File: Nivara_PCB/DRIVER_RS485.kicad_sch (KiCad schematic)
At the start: 0 parts

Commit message: Cambios en el RS485
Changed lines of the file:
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@@
 	(generator_version "9.0")
 	(paper "A4")
+	(hierarchical_label "+3.3V"
+		(shape output)
+		(at 86.36 50.8 0)
+		(effects
+			(font
+				(size 1.27 1.27)
+			)
+			(justify left)
+		)
+	)
 	(hierarchical_label "UART_IN"
 		(shape input)
@@
 		)
 	)
+	(hierarchical_label "+5V"
+		(shape output)
+		(at 73.66 50.8 0)
+		(effects
+			(font
+				(size 1.27 1.27)
+			)
+			(justify left)
+		)
+	)
 	(hierarchical_label "RS485_A"
 		(shape bidirectional)
-		(at 49.53 68.58 0)
+		(at 99.06 60.96 0)
 		(effects
 			(font
@@
 	(hierarchical_label "RS485_B"
 		(shape bidirectional)
-		(at 49.53 71.12 0)
+		(at 99.06 63.5 0)
 		(effects
 			(font

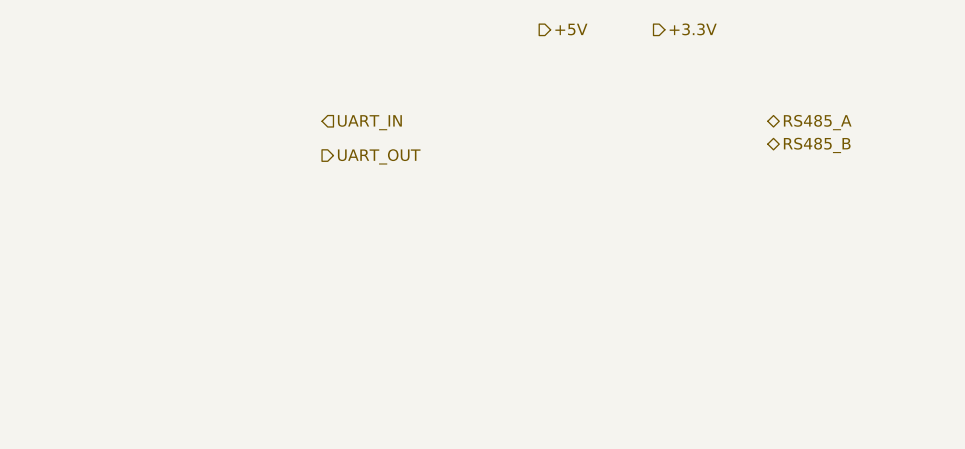
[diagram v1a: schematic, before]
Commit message: Ajuste de RS-485 y protección de alimentación contra cortocircuito y sobre voltaje.
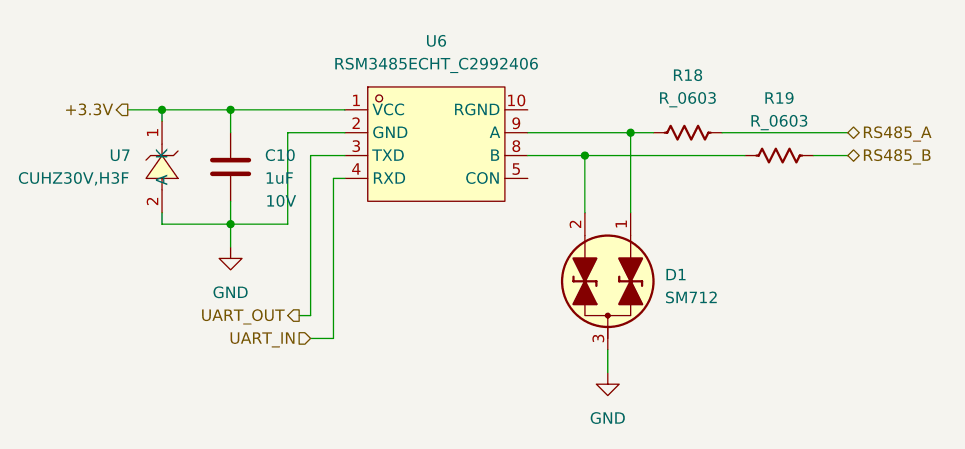
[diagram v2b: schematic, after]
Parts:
- added C10: 1uF, PCM_Capacitor_SMD_AKL:C_0603_1608Metric, symbol PCM_Capacitor_US_AKL:C_0603
- added D1: SM712, PCM_Package_TO_SOT_SMD_AKL:SOT-23, symbol PCM_Diode_TVS_AKL:SM712
- added R18, R19: R_0603, PCM_Resistor_SMD_AKL:R_0603_1608Metric, symbol PCM_Resistor_US_AKL:R_0603
- added U6: RSM3485ECHT_C2992406, EasyEDA:COMM-TH_8P-L19.5-W16.5-P2.54-BL, symbol Fuse_Holder:RSM3485ECHT_C2992406
- added U7: CUHZ30V,H3F, Fuse_Holder:SOD-323HE_L2.0-W1.4-LS2.5-RD, symbol Fuse_Holder:CUHZ30V,H3F
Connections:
- net +3.3V: now also C10.1, U6.1 (VCC), U7.1 (K)
- net RS485_A: now also R18.2
- net RS485_B: now also R19.2
- net UART_IN: now also U6.4 (RXD)
- net UART_OUT: now also U6.3 (TXD)
- new net: D1.2 (A2), R19.1, U6.8 (B)
- new net: D1.1 (A1), R18.1, U6.9 (A)
- new net GND: C10.2, D1.3 (Com), U6.2 (GND), U7.2 (A)
